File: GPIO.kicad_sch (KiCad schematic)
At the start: 12 parts, among them J801 ADC, J802 ADC, M801 Motor_Servo, M802 Motor_Servo, M803 Motor_Servo, M804 Motor_Servo, M805 Motor_Servo, M806 Motor_Servo, M807 Motor_Servo, M808 Motor_Servo

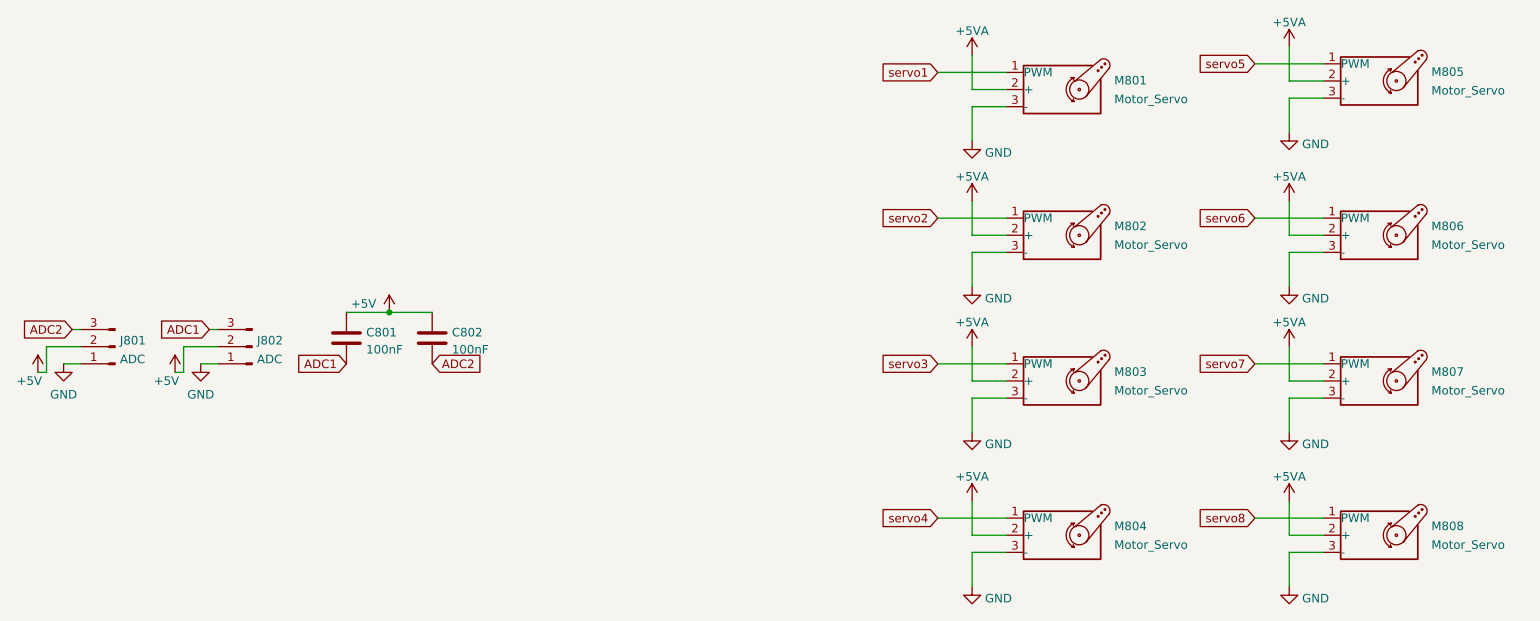
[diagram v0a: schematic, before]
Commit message: altered the code drastically and made a new PCB. PCB is still much work.
I finally fixed that issue where loco functions and speed were not serviced to the multimaus clients.
The Nx code also has been succesfully tested using the monitor.
MCP bug also has been solded. The bug was in assembleIO.py
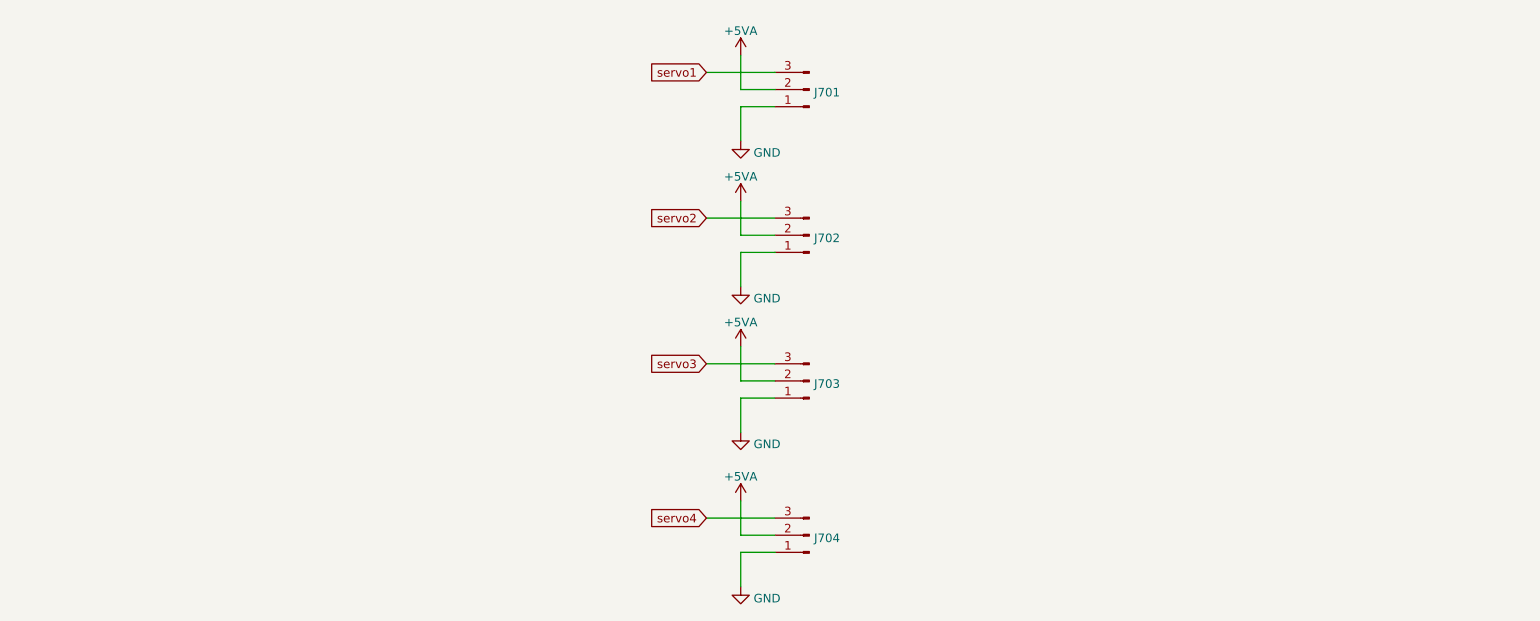
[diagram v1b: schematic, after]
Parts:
- removed C801, C802: 100nF, Capacitor_THT:C_Disc_D3.0mm_W1.6mm_P2.50mm, symbol Device:C
- removed J801, J802: ADC, Connector_PinHeader_2.54mm:PinHeader_1x03_P2.54mm_Vertical, symbol Connector:Conn_01x03_Male
- removed M801, M802, M803, M804, M805, M806, M807, M808: Motor_Servo, Connector_PinHeader_2.54mm:PinHeader_1x03_P2.54mm_Vertical, symbol Motor:Motor_Servo
- added J701: (no value), symbol Connector:Conn_01x03_Male
- added J702, J703, J704: Conn_01x03_Male, symbol Connector:Conn_01x03_Male
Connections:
- net +5VA: now also J701.2 (Pin_2), J702.2 (Pin_2), J703.2 (Pin_2), J704.2 (Pin_2)
- net GND: now also J701.1 (Pin_1), J702.1 (Pin_1), J703.1 (Pin_1), J704.1 (Pin_1)
- net servo1: now also J701.3 (Pin_3)
- net servo2: now also J702.3 (Pin_3)
- net servo3: now also J703.3 (Pin_3)
- net servo4: now also J704.3 (Pin_3)

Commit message: added missing schematics
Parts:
- J701: value (none) -> Conn_01x03_Male; footprint (none) -> Connector_PinHeader_2.54mm:PinHeader_1x03_P2.54mm_Vertical
- J702, J703, J704: footprint (none) -> Connector_PinHeader_2.54mm:PinHeader_1x03_P2.54mm_Vertical
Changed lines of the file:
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@@
       (effects (font (size 1.27 1.27)) (justify right))
     )
-    (property "Value" "" (id 1) (at 140.4112 37.2622 0)
+    (property "Value" "Conn_01x03_Male" (id 1) (at 140.4112 37.2622 0)
       (effects (font (size 1.27 1.27)) (justify right) hide)
     )
-    (property "Footprint" "" (id 2) (at 139.7 35.56 0)
+    (property "Footprint" "Connector_PinHeader_2.54mm:PinHeader_1x03_P2.54mm_Vertical" (id 2) (at 139.7 35.56 0)
       (effects (font (size 1.27 1.27)) hide)
     )
@@
       (effects (font (size 1.27 1.27)) (justify right) hide)
     )
-    (property "Footprint" "" (id 2) (at 139.7 101.6 0)
+    (property "Footprint" "Connector_PinHeader_2.54mm:PinHeader_1x03_P2.54mm_Vertical" (id 2) (at 139.7 101.6 0)
       (effects (font (size 1.27 1.27)) hide)
     )
@@
       (effects (font (size 1.27 1.27)) (justify right) hide)
     )
-    (property "Footprint" "" (id 2) (at 139.7 78.74 0)
+    (property "Footprint" "Connector_PinHeader_2.54mm:PinHeader_1x03_P2.54mm_Vertical" (id 2) (at 139.7 78.74 0)
       (effects (font (size 1.27 1.27)) hide)
     )
@@
       (effects (font (size 1.27 1.27)) (justify right) hide)
     )
-    (property "Footprint" "" (id 2) (at 139.7 57.15 0)
+    (property "Footprint" "Connector_PinHeader_2.54mm:PinHeader_1x03_P2.54mm_Vertical" (id 2) (at 139.7 57.15 0)
       (effects (font (size 1.27 1.27)) hide)
     )

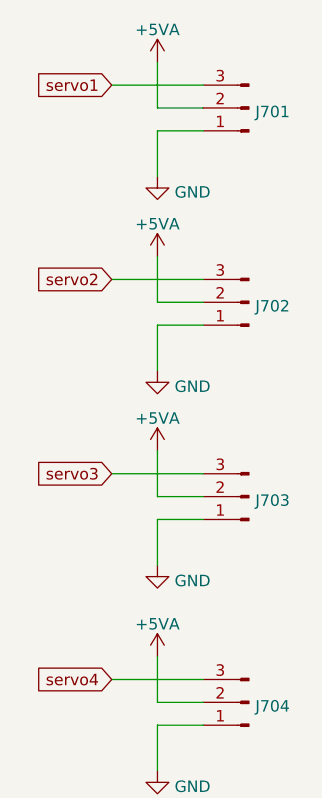
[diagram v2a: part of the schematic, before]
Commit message: replaced the atmega2560 by an stm32
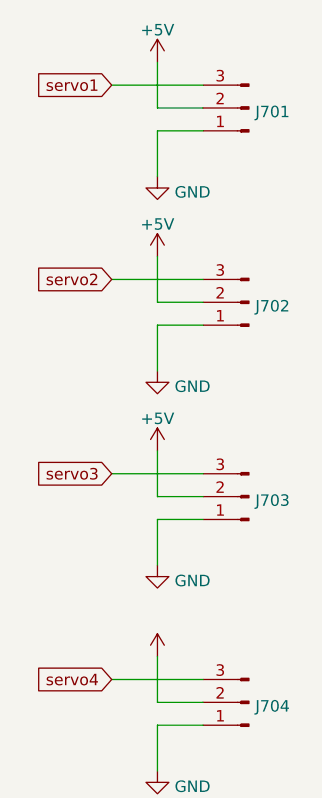
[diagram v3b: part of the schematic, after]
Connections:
- net +5VA renamed +5V
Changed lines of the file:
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@@
     )
-  )
-  (symbol (lib_id "power:+5VA") (at 129.54 96.52 0) (unit 1)
-    (in_bom yes) (on_board yes) (fields_autoplaced)
-    (property "Reference" "#PWR0707" (id 0) (at 129.54 100.33 0)
-      (effects (font (size 1.27 1.27)) hide)
-    )
-    (property "Value" "+5VA" (id 1) (at 129.54 92.9155 0))
-    (property "Footprint" "" (id 2) (at 129.54 96.52 0)
-      (effects (font (size 1.27 1.27)) hide)
-    )
-    (property "Datasheet" "" (id 3) (at 129.54 96.52 0)
-      (effects (font (size 1.27 1.27)) hide)
-    )
-    (pin "1")
   )
   (symbol (lib_id "Connector:Conn_01x03_Male") (at 139.7 35.56 180) (unit 1)
@@
     (pin "1")
   )
-  (symbol (lib_id "power:+5VA") (at 129.54 52.07 0) (unit 1)
-    (in_bom yes) (on_board yes) (fields_autoplaced)
-    (property "Reference" "#PWR0703" (id 0) (at 129.54 55.88 0)
-      (effects (font (size 1.27 1.27)) hide)
-    )
-    (property "Value" "+5VA" (id 1) (at 129.54 48.4655 0))
-    (property "Footprint" "" (id 2) (at 129.54 52.07 0)
-      (effects (font (size 1.27 1.27)) hide)
-    )
-    (property "Datasheet" "" (id 3) (at 129.54 52.07 0)
-      (effects (font (size 1.27 1.27)) hide)
-    )
-    (pin "1")
-  )
   (symbol (lib_id "Connector:Conn_01x03_Male") (at 139.7 101.6 180) (unit 1)
     (in_bom yes) (on_board yes) (fields_autoplaced)
@@
     (pin "3")
   )
-  (symbol (lib_id "power:+5VA") (at 129.54 30.48 0) (unit 1)
+  (symbol (lib_id "power:+5V") (at 129.54 30.48 0) (unit 1)
     (in_bom yes) (on_board yes) (fields_autoplaced)
-    (property "Reference" "#PWR0701" (id 0) (at 129.54 34.29 0)
+    (property "Reference" "#PWR0104" (id 0) (at 129.54 34.29 0)
       (effects (font (size 1.27 1.27)) hide)
     )
-    (property "Value" "+5VA" (id 1) (at 129.54 26.8755 0))
+    (property "Value" "+5V" (id 1) (at 129.54 26.9042 0))
     (property "Footprint" "" (id 2) (at 129.54 30.48 0)
       (effects (font (size 1.27 1.27)) hide)
     )
     (property "Datasheet" "" (id 3) (at 129.54 30.48 0)
+      (effects (font (size 1.27 1.27)) hide)
+    )
+    (pin "1")
+  )
+  (symbol (lib_id "power:+5V") (at 129.54 73.66 0) (unit 1)
+    (in_bom yes) (on_board yes) (fields_autoplaced)
+    (property "Reference" "#PWR0101" (id 0) (at 129.54 77.47 0)
+      (effects (font (size 1.27 1.27)) hide)
+    )
+    (property "Value" "+5V" (id 1) (at 129.54 70.0842 0))
+    (property "Footprint" "" (id 2) (at 129.54 73.66 0)
+      (effects (font (size 1.27 1.27)) hide)
+    )
+    (property "Datasheet" "" (id 3) (at 129.54 73.66 0)
       (effects (font (size 1.27 1.27)) hide)
     )
@@
     (pin "1")
   )
-  (symbol (lib_id "power:+5VA") (at 129.54 73.66 0) (unit 1)
+  (symbol (lib_id "power:+5V") (at 129.54 52.07 0) (unit 1)
     (in_bom yes) (on_board yes) (fields_autoplaced)
-    (property "Reference" "#PWR0705" (id 0) (at 129.54 77.47 0)
+    (property "Reference" "#PWR0103" (id 0) (at 129.54 55.88 0)
       (effects (font (size 1.27 1.27)) hide)
     )
-    (property "Value" "+5VA" (id 1) (at 129.54 70.0555 0))
-    (property "Footprint" "" (id 2) (at 129.54 73.66 0)
+    (property "Value" "+5V" (id 1) (at 129.54 48.4942 0))
+    (property "Footprint" "" (id 2) (at 129.54 52.07 0)
       (effects (font (size 1.27 1.27)) hide)
     )
-    (property "Datasheet" "" (id 3) (at 129.54 73.66 0)
+    (property "Datasheet" "" (id 3) (at 129.54 52.07 0)
       (effects (font (size 1.27 1.27)) hide)
     )
+    (pin "1")
+  )
+  (symbol (lib_id "power:+5V") (at 129.54 96.52 0) (unit 1)
+    (in_bom yes) (on_board yes) (fields_autoplaced)
+    (property "Reference" "#PWR0102" (id 0) (at 129.54 100.33 0)
+      (effects (font (size 1.27 1.27)) hide)
+    )
+    (property "Value" "" (id 1) (at 129.54 92.9442 0))
+    (property "Footprint" "" (id 2) (at 129.54 96.52 0)
+      (effects (font (size 1.27 1.27)) hide)
+    )
+    (property "Datasheet" "" (id 3) (at 129.54 96.52 0)
+      (effects (font (size 1.27 1.27)) hide)
+    )
